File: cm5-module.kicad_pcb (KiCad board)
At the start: 4 copper layers, 100 x 100 mm, 71 parts, among them J1 DIN-41612-connector_090319679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, J10 Bus_M.2_1-2199230-6, J3 USB-A_USB-303WSD-BRY, J4 USB-C_USB-310F-B-SU, J5 HDMI_A, J6 MicroSD_5033981892, J7 CM5_101-200_3mm-stack, J8 RJ45_HC612601A-M893-A, J9 CM5_1-100_3mm-stack, U1 CH334P, U2 FT230XQ-R, U5 AP22615AWU-7, U6 AP22615AWU-7, Y1 Oscillator_32.768kHz_OK2EL89C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, Y2 X322512MSB4SI

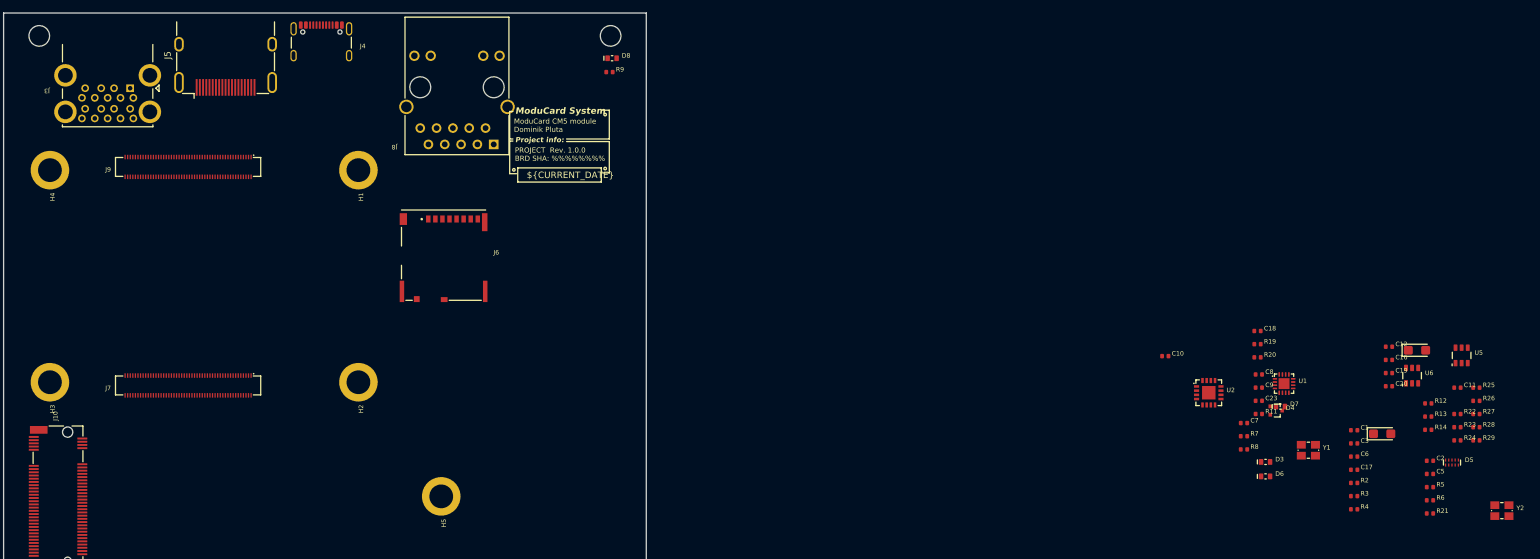
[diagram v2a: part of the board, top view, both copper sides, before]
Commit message: [#1] Add level shifter for UART debug, update footprints from library
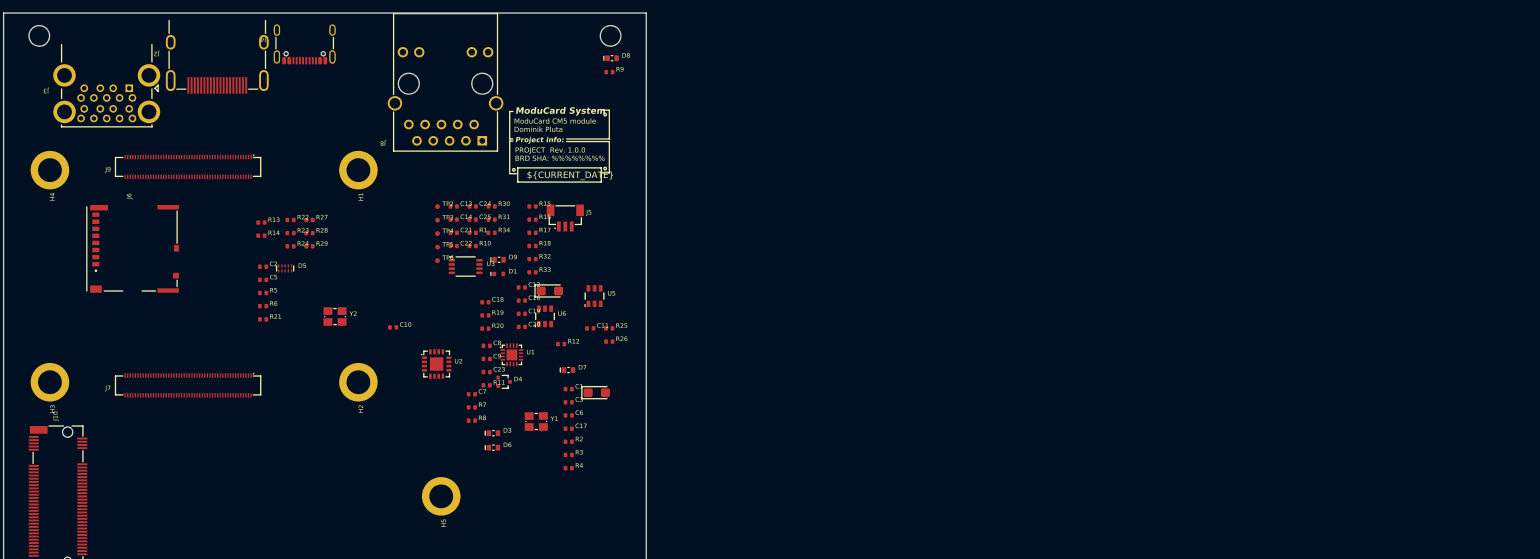
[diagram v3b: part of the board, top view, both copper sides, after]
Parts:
- added C13: C-4u7-0402, DW-footprints:C_0402_1005Metric, F.Cu at (109.4, 81.4)
- added C14: C-100n-0402, DW-footprints:C_0402_1005Metric, F.Cu at (109.4, 83.4)
- added C21: C-47p-0402, DW-footprints:C_0402_1005Metric, F.Cu at (109.4, 85.5)
- added C22: C-47p-0402, DW-footprints:C_0402_1005Metric, F.Cu at (109.4, 87.5)
- added C24: C-100n-0402, DW-footprints:C_0402_1005Metric, F.Cu at (112.4, 81.4)
- added C25: C-100n-0402, DW-footprints:C_0402_1005Metric, F.Cu at (112.4, 83.4)
- added D1: PESD5Z5, DW-footprints:D_SOD-523, F.Cu at (116.4, 91.9)
- added D9: LED-R-0603_KT-0603R, DW-footprints:LED_0603_1608Metric_R, F.Cu at (116.5, 89.7)
- added J2: HDMI-A_HDMI-19PIN-043, DW-footprints:Conn_HDMI-A_HDMI-19PIN-043, F.Cu at (72.6, 57.2)
- added R1: R-22R-0402, DW-footprints:R_0402_1005Metric, F.Cu at (112.4, 85.5)
- added R10: R-22R-0402, DW-footprints:R_0402_1005Metric, F.Cu at (112.4, 87.5)
- added R15: R-0R-0402, DW-footprints:R_0402_1005Metric, F.Cu at (121.7, 81.4)
- added R16: R-0R-0402, DW-footprints:R_0402_1005Metric, F.Cu at (121.7, 83.4)
- added R17: R-0R-0402, DW-footprints:R_0402_1005Metric, F.Cu at (121.7, 85.5)
- added R18: R-0R-0402, DW-footprints:R_0402_1005Metric, F.Cu at (121.7, 87.5)
- added R30: R-1k-0402, DW-footprints:R_0402_1005Metric, F.Cu at (115.3, 81.4)
- added R31: R-0R-0402, DW-footprints:R_0402_1005Metric, F.Cu at (115.3, 83.4)
- added R32: R-0R-0402, DW-footprints:R_0402_1005Metric, F.Cu at (121.7, 89.6)
- added R33: R-0R-0402, DW-footprints:R_0402_1005Metric, F.Cu at (121.7, 91.6)
- added R34: R-0R-0402, DW-footprints:R_0402_1005Metric, F.Cu at (115.3, 85.5)
- added TP2: TP_SMD_0.75mm, DW-footprints:TP_SMD_0.75mm, F.Cu at (106.9, 81.4)
- added TP3: TP_SMD_0.75mm, DW-footprints:TP_SMD_0.75mm, F.Cu at (106.9, 83.5)
- added TP4: TP_SMD_0.75mm, DW-footprints:TP_SMD_0.75mm, F.Cu at (106.9, 85.6)
- added TP5: TP_SMD_0.75mm, DW-footprints:TP_SMD_0.75mm, F.Cu at (106.9, 87.7)
- added TP6: TP_SMD_0.75mm, DW-footprints:TP_SMD_0.75mm, F.Cu at (106.9, 89.8)
- added U3: NTS0102DP, DW-footprints:TSSOP-8_3x3mm_P0.65mm, F.Cu at (111.3, 90.7)
- J4: footprint DW-footprints:USB-C-Receptacle_USB-310F-B-SU -> DW-footprints:USB-C-Receptacle_USB-310-B-SU
- J5: value HDMI_A -> JST_SH_1x3_BM03B-SRSS-TB-LF-SN; footprint Connector_Video:HDMI_A_Molex_208658-1001_Horizontal -> DW-footprints:Conn_JST_SH_1x3_BM03B-SRSS-TB
- moved C2 184.1 mm to (79.8, 90.8)
- moved C5 184.1 mm to (79.8, 92.8)
- moved D5 184.1 mm to (83.2, 91.0)
- moved R13 184.1 mm to (79.5, 83.9)
- moved R14 184.1 mm to (79.5, 85.9)
- moved R21 184.1 mm to (79.8, 99.0)
- moved R22 184.1 mm to (84.0, 83.5)
- moved R23 184.1 mm to (84.0, 85.5)
- moved R24 184.1 mm to (84.0, 87.6)
- moved R5 184.1 mm to (79.8, 94.9)
- moved R6 184.1 mm to (79.8, 96.9)
- moved Y2 184.1 mm to (90.9, 98.5)
- moved R27 184.1 mm to (87.0, 83.5)
- moved R28 184.1 mm to (87.0, 85.5)
- moved R29 184.1 mm to (87.0, 87.6)
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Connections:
- net /CM5/PCIe_M2.REFCLK+ renamed /CM5/PCIe.REFCLK+
- net /CM5/PCIe_M2.REFCLK- renamed /CM5/PCIe.REFCLK-
- net /CM5/PCIe_M2.RX0+ renamed /CM5/PCIe.RX0+
- net /CM5/PCIe_M2.RX0- renamed /CM5/PCIe.RX0-
- net /CM5/PCIe_M2.TX0+ renamed /CM5/PCIe.TX0+
- net /CM5/PCIe_M2.TX0- renamed /CM5/PCIe.TX0-
- net /CM5/~{PCIe_M2_CLKREQ} renamed /CM5/~{PCIe_CLKREQ}
- net /CM5/~{PCIe_M2_PERST} renamed /CM5/~{PCIe_PERST}
- net /CM5/~{PCIe_M2_PWR_EN} renamed /CM5/~{PCIe_PWR_EN}
- net /CM5/~{PCIe_M2_WAKE} renamed /CM5/~{PCIe_WAKE}
- net Net-(J9-+1.8v_(Output)-Pad88) renamed /CM5/+1V8_CM5
- net Net-(J9-+3.3v_(Output)-Pad84) renamed /CM5/+3V3_CM5
- J5 pad 1: /CM5/HDMI_0.D2+ -> /CM5/CM5_RX
- J5 pad 3: /CM5/HDMI_0.D2- -> /CM5/CM5_TX
- J9 pad 34: unconnected-(J9-GPIO5-Pad34) -> /CM5/UART2_RX
- J9 pad 54: unconnected-(J9-GPIO4-Pad54) -> /CM5/UART2_TX
- J9 pad 78: unconnected-(J9-GPIO_VREF(1.8v/3.3v_IN)-Pad78) -> /CM5/GPIO_VREF
- U2 pad 15: /USB console/FTDI_TX -> Net-(U2-TXD)
- U2 pad 2: /USB console/FTDI_RX -> Net-(U2-RXD)
- U2 pad 6: /USB console/USB_D+ -> Net-(U2-D+)
- U2 pad 7: /USB console/USB_D- -> Net-(U2-D-)
- U2 pad 9: unconnected-(U2-~{RESET}-Pad9) -> /USB console/FTDI_VCCIO

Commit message: [#1] Sync PCB with schematic, draft component placement
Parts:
- removed the C5 at (79.8, 92.8)
- added A2: M.2 M-key 2280, DW-footprints:Card_M.2-2280-M-key, F.Cu at (127.5, 126.5)
- added C27: C-100n-0402, DW-footprints:C_0402_1005Metric, F.Cu at (116.3, 113.0)
- added C28: C-10u-0603, DW-footprints:C_0603_1608Metric, F.Cu at (116.9, 108.1)
- added C29: C-10u-0603, DW-footprints:C_0603_1608Metric, F.Cu at (119.6, 108.1)
- added C30: C-10u-0603, DW-footprints:C_0603_1608Metric, F.Cu at (122.3, 108.1)
- added C31: C-10u-0603, DW-footprints:C_0603_1608Metric, F.Cu at (123.7, 108.1)
- added C32: C-10u-0603, DW-footprints:C_0603_1608Metric, F.Cu at (118.3, 108.1)
- added C33: C-10u-0603, DW-footprints:C_0603_1608Metric, F.Cu at (121.0, 108.1)
- added C34: C-4u7-0402, DW-footprints:C_0402_1005Metric, F.Cu at (113.2, 113.0)
- added C35: C-1u-0402, DW-footprints:C_0402_1005Metric, F.Cu at (114.2, 113.0)
- added C36: C-10u-0603, DW-footprints:C_0603_1608Metric, F.Cu at (119.6, 110.6)
- added C37: C-10u-0603, DW-footprints:C_0603_1608Metric, F.Cu at (118.3, 110.6)
- added C38: C-10u-0603, DW-footprints:C_0603_1608Metric, F.Cu at (121.0, 110.6)
- added C39: C-100n-0402, DW-footprints:C_0402_1005Metric, F.Cu at (117.1, 110.6)
- added C40: C-100n-0402, DW-footprints:C_0402_1005Metric, F.Cu at (111.2, 85.9)
- added C41: C-100n-0402, DW-footprints:C_0402_1005Metric, F.Cu at (117.6, 85.9)
- added C42: C-10u-0603, DW-footprints:C_0603_1608Metric, F.Cu at (107.7, 108.2)
- added C43: C-100n-0402, DW-footprints:C_0402_1005Metric, F.Cu at (106.4, 108.2)
- added C44: C-10u-0603, DW-footprints:C_0603_1608Metric, F.Cu at (101.8, 108.2)
- added C45: C-10u-0603, DW-footprints:C_0603_1608Metric, F.Cu at (103.2, 108.2)
- added L1: L-1u-20A-CJiang-FEXL0650A, DW-footprints:L-CJiang-FEXL0650A, F.Cu at (113.7, 103.3)
- added L2: L-1u-20A-CJiang-FEXL0650A, DW-footprints:L-CJiang-FEXL0650A, F.Cu at (104.7, 103.2)
- added Q1: SIS472DN-T1-GE3, DW-footprints:PowerPAK-1212-8_Single, F.Cu at (113.4, 81.7)
- added Q2: SIS472DN-T1-GE3, DW-footprints:PowerPAK-1212-8_Single, F.Cu at (119.8, 81.7)
- added Q3: AO3400A, DW-footprints:SOT-23-3, F.Cu at (119.8, 89.4)
- added R35: R-499k-0402, DW-footprints:R_0402_1005Metric, F.Cu at (115.3, 113.0)
- added R36: R-499k-0402, DW-footprints:R_0402_1005Metric, F.Cu at (112.1, 113.0)
- added R37: R-10k-0402, DW-footprints:R_0402_1005Metric, F.Cu at (109.0, 113.0)
- added R38: R-73k2-0402, DW-footprints:R_0402_1005Metric, F.Cu at (110.0, 113.0)
- added R39: R-10k-0402, DW-footprints:R_0402_1005Metric, F.Cu at (111.1, 113.0)
- added R40: R-10k-0402, DW-footprints:R_0402_1005Metric, F.Cu at (110.2, 85.9)
- added R41: R-10k-0402, DW-footprints:R_0402_1005Metric, F.Cu at (116.5, 85.9)
- added R42: R-10k-0402, DW-footprints:R_0402_1005Metric, F.Cu at (104.9, 111.1)
- added R43: R-10k-0402, DW-footprints:R_0402_1005Metric, F.Cu at (104.9, 110.0)
- added TP7: TP_SMD_0.75mm, DW-footprints:TP_SMD_0.75mm, F.Cu at (87.1, 86.8)
- added U6: LM74700QDBVRQ1, DW-footprints:SOT-23-6, F.Cu at (113.4, 85.9)
- added U7: SIC431AED-T1-GE3, DW-footprints:MLP44-24L_4x4x0.75mm, F.Cu at (113.7, 109.4)
- added U8: LM74700QDBVRQ1, DW-footprints:SOT-23-6, F.Cu at (119.8, 85.9)
- added U9: TPS564247DRLR, DW-footprints:SOT-563, F.Cu at (104.9, 108.2)
- moved R7 120.0 mm to (43.2, 139.3)
- moved D2 119.8 mm to (45.8, 139.3)
- moved C1 78.6 mm to (55.3, 122.7), turned to 180 degrees
- moved Y1 67.1 mm to (55.4, 120.2), turned to 90 degrees
- moved D6 59.3 mm to (91.2, 64.8), turned to 90 degrees
- moved D5 56.7 mm to (92.6, 64.8), turned to 90 degrees
- moved R20 55.8 mm to (92.5, 62.5), turned to 90 degrees
- moved R21 54.3 mm to (91.4, 62.5), turned to 90 degrees
- moved J4 53.3 mm to (75.6, 67.8)
- moved R5 49.6 mm to (74.6, 71.7), turned to -90 degrees
- moved C24 49.6 mm to (54.6, 80.3), turned to 180 degrees
- moved R4 49.3 mm to (73.3, 71.8), turned to 90 degrees
- moved R28 49.1 mm to (133.1, 84.9), turned to 180 degrees
- moved R27 49.1 mm to (133.1, 83.8), turned to 180 degrees
- moved C3 48.4 mm to (84.4, 89.5)
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- renumbered C11 to C1, C15 to C10, C19 to C11, C16 to C12, C21 to C13, C22 to C14, C13 to C15, C14 to C16, C7 to C17, C24 to C18, C25 to C19, C18 to C2, C2 to C20, C9 to C21, C23 to C22, C8 to C23, C10 to C24, C1 to C4, C4 to C5, C17 to C6, C6 to C7, C12 to C8, C20 to C9, D4 to D1, D8 to D2, D1 to D3, D5 to D4, D3 to D5, D9 to D7, D7 to D8, J6 to J10, J9 to J2, J7 to J3, J5 to J4, J10 to J5, J8 to J6, J3 to J7, J2 to J8, J4 to J9, R32 to R1, R2 to R10, R3 to R11, R4 to R12, R12 to R14, R14 to R15, R31 to R16, R34 to R17, R1 to R18, R10 to R19, R33 to R2, R8 to R20, R7 to R21, R30 to R22, R5 to R23, R21 to R24, R6 to R25, R11 to R26, R22 to R27, R23 to R28, R24 to R29, R16 to R3, R25 to R30, R26 to R31, R27 to R32, R28 to R33, R29 to R34, R15 to R4, R18 to R5, R17 to R6, R9 to R7, R19 to R8, R20 to R9, TP4 to TP2, TP5 to TP3, TP2 to TP4, TP3 to TP5, U5 to U1, U6 to U2, U2 to U3, U3 to U4, U1 to U5
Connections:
- D4 pad 1: /USB console/USB_D- -> /USB console/CC2
- D4 pad 10: /USB console/USB_D- -> /USB console/CC2
- D4 pad 2: /USB console/USB_D+ -> /USB console/USB_D-
- D4 pad 4: /USB console/CC2 -> /USB console/USB_D+
- D4 pad 7: /USB console/CC2 -> /USB console/USB_D+
- D4 pad 9: /USB console/USB_D+ -> /USB console/USB_D-
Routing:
- net GND: track 0.00 -> 0.76 mm, vias 0 -> 1
- net /CM5/ETH.D4+: track 0.76 -> 0.00 mm, vias 1 -> 0

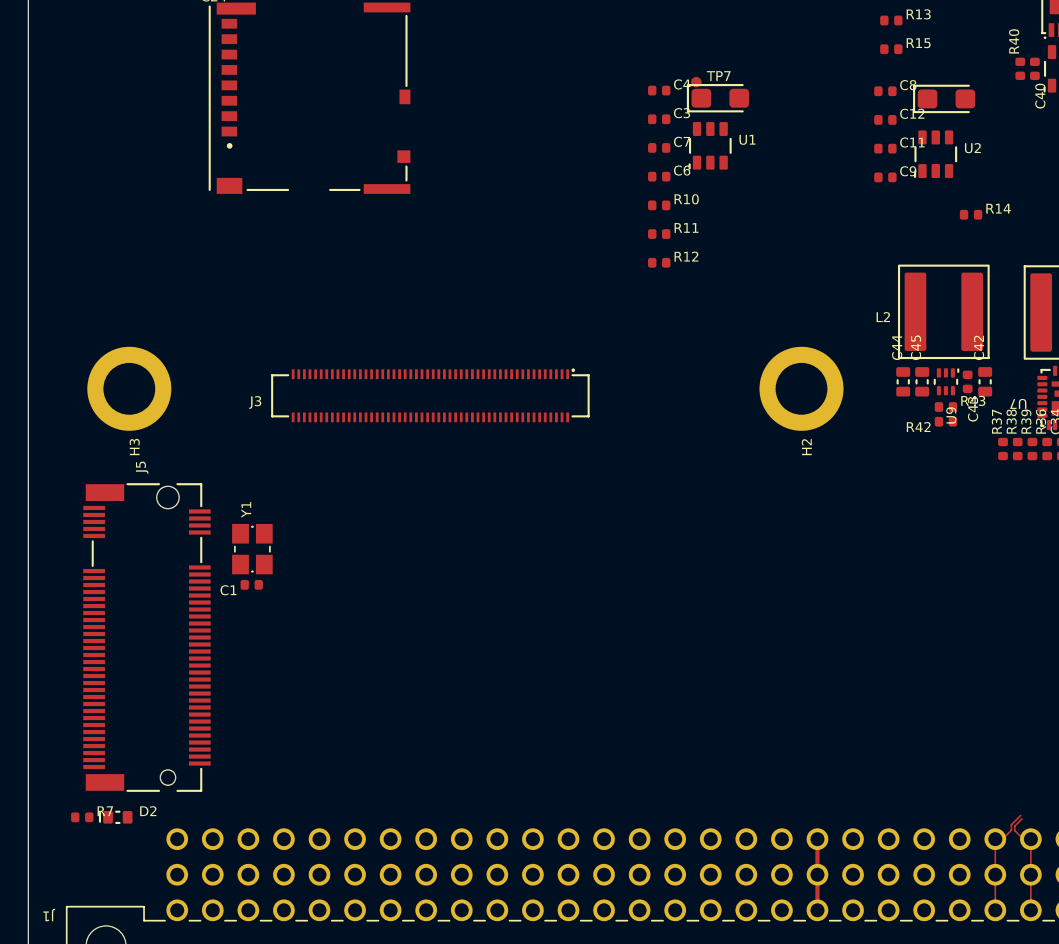
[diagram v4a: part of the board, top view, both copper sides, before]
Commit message: [#1] WIP: Refactor schematic
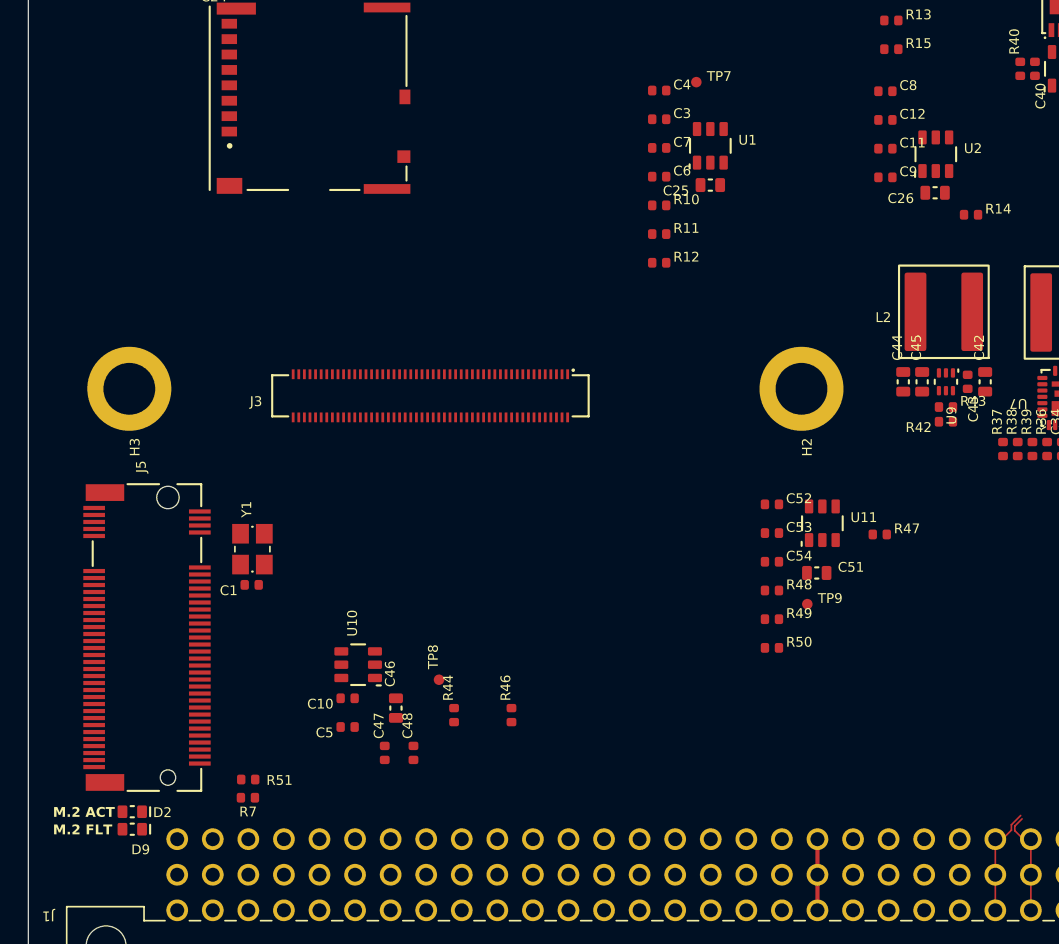
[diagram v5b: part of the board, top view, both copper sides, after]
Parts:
- added C25: C-10u-0603, DW-footprints:C_0603_1608Metric, F.Cu at (88.1, 94.2)
- added C26: C-10u-0603, DW-footprints:C_0603_1608Metric, F.Cu at (104.1, 94.7)
- added C46: C-10u-0603, DW-footprints:C_0603_1608Metric, F.Cu at (65.6, 131.5)
- added C47: C-4u7-0402, DW-footprints:C_0402_1005Metric, F.Cu at (64.8, 134.7)
- added C48: C-100n-0402, DW-footprints:C_0402_1005Metric, F.Cu at (66.9, 134.7)
- added C51: C-10u-0603, DW-footprints:C_0603_1608Metric, F.Cu at (95.7, 121.9)
- added C52: C-4u7-0402, DW-footprints:C_0402_1005Metric, F.Cu at (92.5, 117.0)
- added C53: C-4u7-0402, DW-footprints:C_0402_1005Metric, F.Cu at (92.5, 119.0)
- added C54: C-100n-0402, DW-footprints:C_0402_1005Metric, F.Cu at (92.5, 121.1)
- added D9: LED-R-0603_KT-0603R, DW-footprints:LED_0603_1608Metric_R, F.Cu at (46.8, 140.2)
- added R44: R-0R-0402, DW-footprints:R_0402_1005Metric, F.Cu at (69.8, 132.0)
- added R46: R-2k2-0402, DW-footprints:R_0402_1005Metric, F.Cu at (73.9, 132.0)
- added R47: R-0R-0402, DW-footprints:R_0402_1005Metric, F.Cu at (100.2, 119.1)
- added R48: R-10k-0402, DW-footprints:R_0402_1005Metric, F.Cu at (92.5, 123.1)
- added R49: R-10k-0402, DW-footprints:R_0402_1005Metric, F.Cu at (92.5, 125.2)
- added R50: R-0R-0402, DW-footprints:R_0402_1005Metric, F.Cu at (92.5, 127.2)
- added R51: R-1k-0402, DW-footprints:R_0402_1005Metric, F.Cu at (55.1, 136.6)
- added TP8: TP_SMD_0.75mm, DW-footprints:TP_SMD_0.75mm, F.Cu at (68.7, 129.5)
- added TP9: TP_SMD_0.75mm, DW-footprints:TP_SMD_0.75mm, F.Cu at (95.0, 124.1)
- added U10: AP22615AWU-7, DW-footprints:TSOT-23-6, F.Cu at (62.9, 128.4)
- added U11: AP22615AWU-7, DW-footprints:TSOT-23-6, F.Cu at (96.1, 118.3)
- C10: value 10uF -> C-4u7-0402; footprint PCM_JLCPCB:C_CASE-A-3216-18(mm) -> DW-footprints:C_0402_1005Metric
- C5: value 10uF -> C-100n-0402; footprint PCM_JLCPCB:C_CASE-A-3216-18(mm) -> DW-footprints:C_0402_1005Metric
- moved C10 60.5 mm to (62.2, 130.8), turned to 180 degrees
- moved C5 52.2 mm to (62.2, 132.9), turned to 180 degrees
- moved R7 11.9 mm to (55.0, 137.9), turned to 180 degrees
- moved D2 1.10 mm to (46.8, 138.9), turned to 180 degrees
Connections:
- net Net-(Q3-G) renamed /Power/5V
- C10 pad 1: /HDMI/HDMI_+5V -> GND
- C10 pad 2: GND -> +3V3
- C24 pad 2: +3V3 -> Net-(J10-VDD)
- C36 pad 2: /Power/12V_IN -> +12V
- C37 pad 2: /Power/12V_IN -> +12V
- C38 pad 2: /Power/12V_IN -> +12V
- C39 pad 1: /Power/12V_IN -> +12V
- C5 pad 1: /2xUSB3.0/+VBUS -> +3V3
- J10 pad 4: +3V3 -> Net-(J10-VDD)
- J2 pad 73: /CM5/SD_VDD_Override -> unconnected-(J2-SD_VDD_Override-Pad73)
- J3 pad 6: /CM5/~{PCIe_PWR_EN} -> /CM5/PCIe_PWR_EN
- J5 pad 68: /M.2/SUSCLK -> /M.2/SUSCLK_R
- R31 pad 1: /USB hub/USB_3.D+ -> /Backplane/BACKPLANE.D+
- R32 pad 1: /USB hub/USB_3.D- -> /Backplane/BACKPLANE.D-
- R33 pad 1: /Backplane/BACKPLANE.D+ -> /USB hub/USB_4.D+
- R34 pad 1: /Backplane/BACKPLANE.D- -> /USB hub/USB_4.D-
- R39 pad 2: /Power/12V_IN -> +12V
- U7 pad 1: /Power/12V_IN -> +12V
- U7 pad 2: /Power/12V_IN -> +12V
- U7 pad 22: /Power/12V_IN -> +12V
- U7 pad 26: /Power/12V_IN -> +12V
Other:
- board text added: "M.2 ACT"
- board text added: "M.2 FLT"
